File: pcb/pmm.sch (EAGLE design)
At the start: 38 parts, among them IC3 STM32F042F4, J1 AUDIO_JACK_3.5MM_PTH, J2 FFC3B07-05-T, SW3 324_SW, SW4 324_SW, U2 USBC_16P, U4 XC6206_DEV

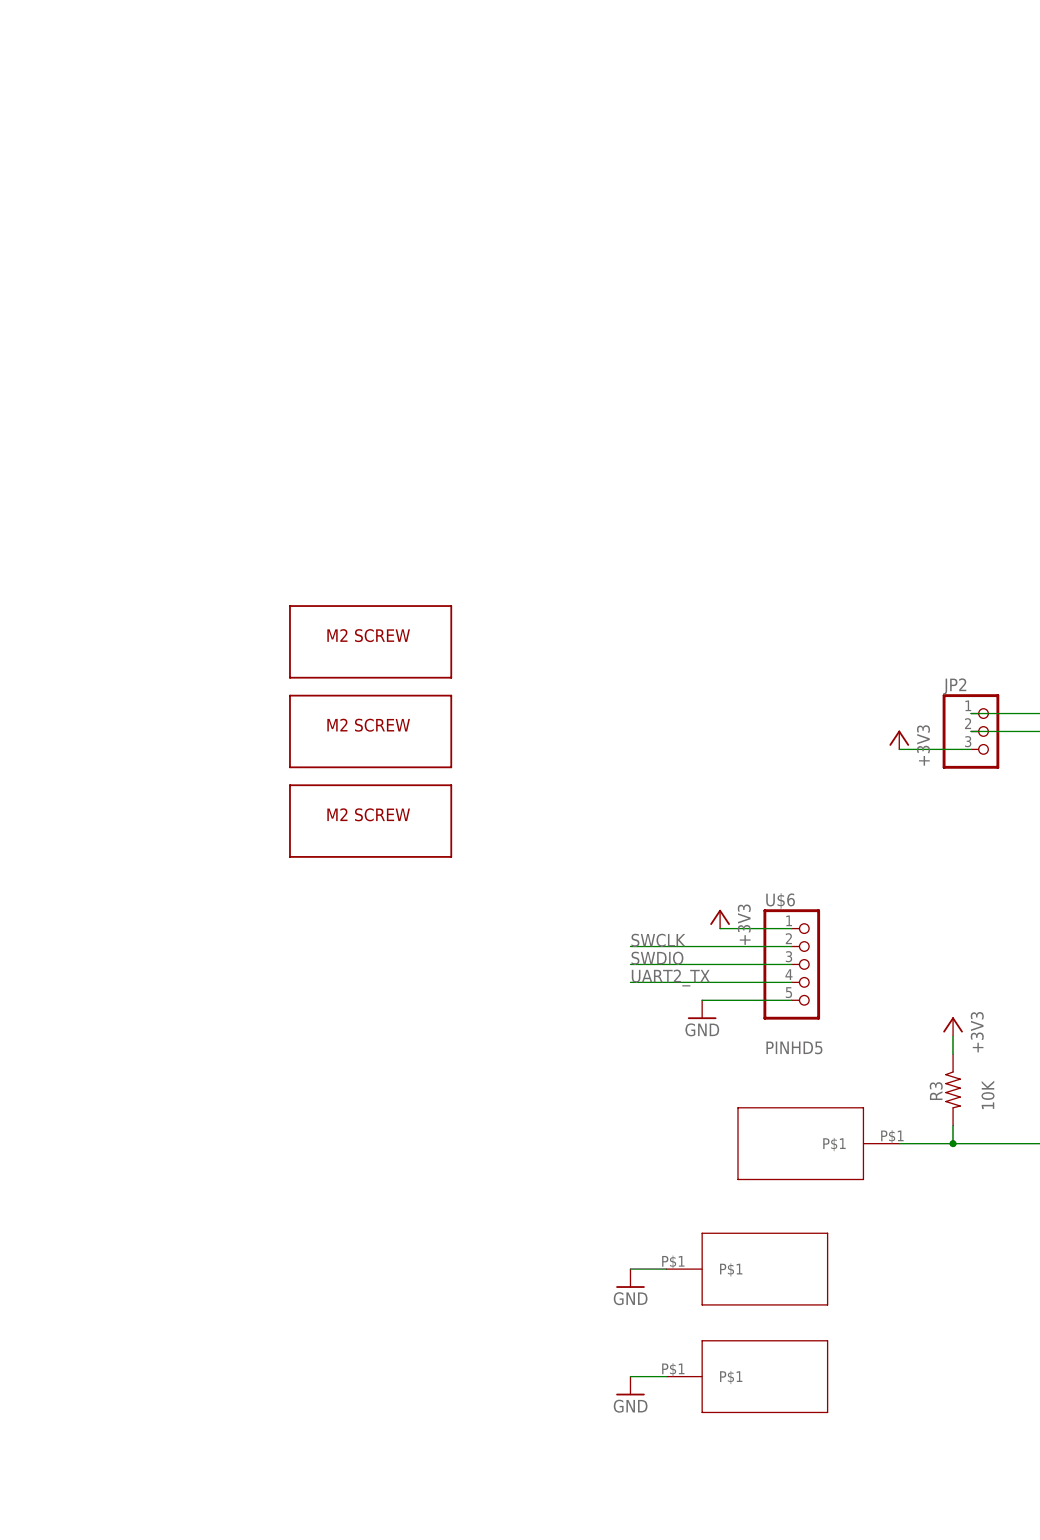
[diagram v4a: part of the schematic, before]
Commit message: added spring contacts
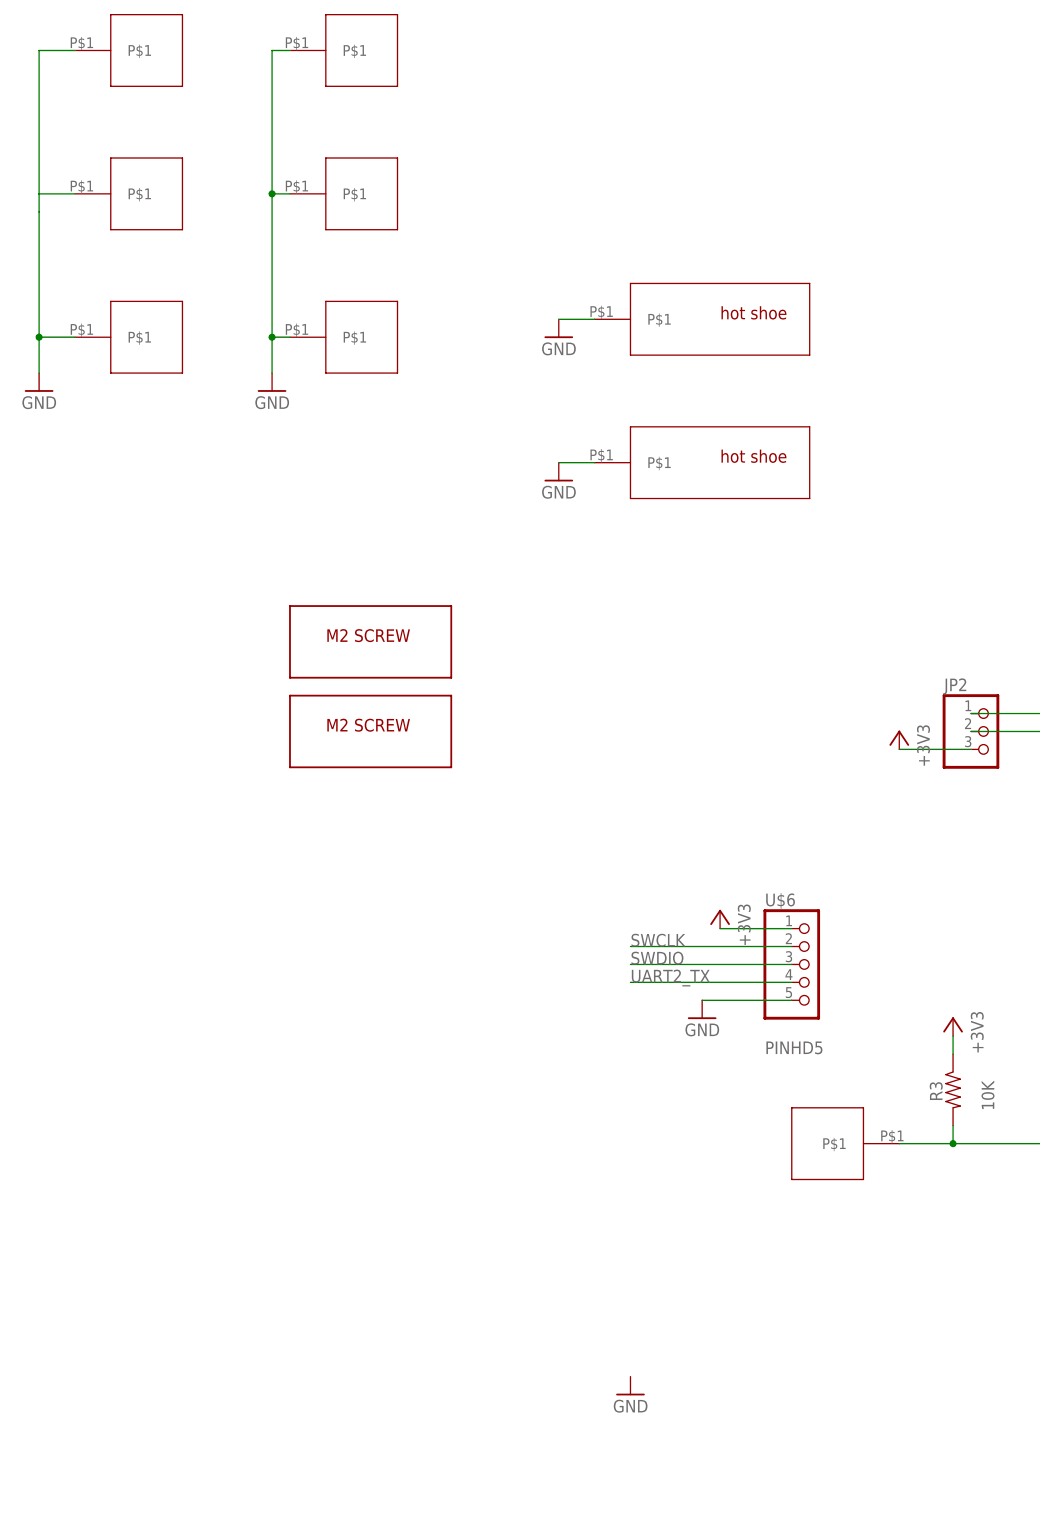
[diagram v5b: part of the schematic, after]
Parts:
- removed U$3: POGO_TH001, apricot:POGO_TH001
- added U$10, U$15: HOTSHOE, apricot:HOTSHOE
- added U$11, U$13, U$14, U$9: SPRING_CONTACT, apricot:SPRING_CONTACT
- U$2: value M2_SCREW_DEV -> SPRING_CONTACT; device 3pos_slide_switch_centered:M2_SCREW_DEV -> apricot:SPRING_CONTACT
- U$4, U$5: value POGO_TH001 -> SPRING_CONTACT; device apricot:POGO_TH001 -> apricot:SPRING_CONTACT
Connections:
- net GND: now also U$10.P$1, U$11.P$1, U$13.P$1, U$14.P$1, U$15.P$1, U$9.P$1
- net N$2: now also U$2.P$1; no longer U$3.P$1
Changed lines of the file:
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@@
 <part name="U$12" library="3pos_slide_switch_centered" deviceset="M2_SCREW_DEV" device=""/>
 <part name="U$1" library="3pos_slide_switch_centered" deviceset="M2_SCREW_DEV" device=""/>
-<part name="U$2" library="3pos_slide_switch_centered" deviceset="M2_SCREW_DEV" device=""/>
-<part name="U$3" library="apricot" deviceset="POGO_TH001" device=""/>
-<part name="U$4" library="apricot" deviceset="POGO_TH001" device=""/>
-<part name="U$5" library="apricot" deviceset="POGO_TH001" device=""/>
 <part name="U1" library="lul" deviceset="LUL_DISP_OLED_UG-2864HSWEG01" device=""/>
 <part name="GND26" library="supply1" library_urn="urn:adsk.eagle:library:371" deviceset="GND" device=""/>
@@
 <part name="R9" library="joyAnalog" deviceset="RESISTOR" device="0805-RES" value="10K"/>
 <part name="GND21" library="supply1" deviceset="GND" device=""/>
+<part name="U$11" library="apricot" deviceset="SPRING_CONTACT" device=""/>
+<part name="U$13" library="apricot" deviceset="SPRING_CONTACT" device=""/>
+<part name="U$14" library="apricot" deviceset="SPRING_CONTACT" device=""/>
+<part name="U$4" library="apricot" deviceset="SPRING_CONTACT" device=""/>
+<part name="U$5" library="apricot" deviceset="SPRING_CONTACT" device=""/>
+<part name="U$9" library="apricot" deviceset="SPRING_CONTACT" device=""/>
+<part name="GND22" library="supply1" deviceset="GND" device=""/>
+<part name="U$10" library="apricot" deviceset="HOTSHOE" device=""/>
+<part name="U$15" library="apricot" deviceset="HOTSHOE" device=""/>
+<part name="GND23" library="supply1" deviceset="GND" device=""/>
+<part name="GND24" library="supply1" deviceset="GND" device=""/>
+<part name="U$2" library="apricot" deviceset="SPRING_CONTACT" device=""/>
 </parts>
 <sheets>
@@
 <instance part="U$12" gate="G$1" x="-144.78" y="78.74" smashed="yes"/>
 <instance part="U$1" gate="G$1" x="-144.78" y="66.04" smashed="yes"/>
-<instance part="U$2" gate="G$1" x="-144.78" y="53.34" smashed="yes"/>
-<instance part="U$3" gate="G$1" x="-81.28" y="7.62" smashed="yes" rot="R180"/>
-<instance part="U$4" gate="G$1" x="-88.9" y="-10.16" smashed="yes"/>
-<instance part="U$5" gate="G$1" x="-88.9" y="-25.4" smashed="yes"/>
 <instance part="U1" gate="G$1" x="60.96" y="137.16" smashed="yes">
 <attribute name="NAME" x="40.64" y="162.56" size="1.27" layer="95" font="vector"/>
@@
 <attribute name="VALUE" x="-5.08" y="53.34" size="1.778" layer="96"/>
 </instance>
-<instance part="GND2" gate="1" x="-106.68" y="-12.7" smashed="yes" rot="MR0">
-<attribute name="VALUE" x="-104.14" y="-15.24" size="1.778" layer="96" rot="MR0"/>
+<instance part="GND2" gate="1" x="-190.5" y="114.3" smashed="yes" rot="MR0">
+<attribute name="VALUE" x="-187.96" y="111.76" size="1.778" layer="96" rot="MR0"/>
 </instance>
 <instance part="GND3" gate="1" x="-106.68" y="-27.94" smashed="yes" rot="MR0">
@@
 <attribute name="VALUE" x="-25.4" y="53.34" size="1.778" layer="96" rot="MR0"/>
 </instance>
+<instance part="U$11" gate="G$1" x="-175.26" y="142.24" smashed="yes"/>
+<instance part="U$13" gate="G$1" x="-175.26" y="121.92" smashed="yes"/>
+<instance part="U$14" gate="G$1" x="-175.26" y="162.56" smashed="yes"/>
+<instance part="U$4" gate="G$1" x="-144.78" y="142.24" smashed="yes"/>
+<instance part="U$5" gate="G$1" x="-144.78" y="121.92" smashed="yes"/>
+<instance part="U$9" gate="G$1" x="-144.78" y="162.56" smashed="yes"/>
+<instance part="GND22" gate="1" x="-157.48" y="114.3" smashed="yes" rot="MR0">
+<attribute name="VALUE" x="-154.94" y="111.76" size="1.778" layer="96" rot="MR0"/>
+</instance>
+<instance part="U$10" gate="G$1" x="-101.6" y="124.46" smashed="yes"/>
+<instance part="U$15" gate="G$1" x="-101.6" y="104.14" smashed="yes"/>
+<instance part="GND23" gate="1" x="-116.84" y="101.6" smashed="yes" rot="MR0">
+<attribute name="VALUE" x="-114.3" y="99.06" size="1.778" layer="96" rot="MR0"/>
+</instance>
+<instance part="GND24" gate="1" x="-116.84" y="121.92" smashed="yes" rot="MR0">
+<attribute name="VALUE" x="-114.3" y="119.38" size="1.778" layer="96" rot="MR0"/>
+</instance>
+<instance part="U$2" gate="G$1" x="-78.74" y="7.62" smashed="yes" rot="R180"/>
 </instances>
 <busses>
@@
 <pinref part="R8" gate="G$1" pin="2"/>
 <pinref part="GND30" gate="1" pin="GND"/>
-</segment>
-<segment>
-<pinref part="GND2" gate="1" pin="GND"/>
-<pinref part="U$4" gate="G$1" pin="P$1"/>
-<wire x1="-106.68" y1="-10.16" x2="-101.6" y2="-10.16" width="0.1524" layer="91"/>
-</segment>
-<segment>
-<pinref part="GND3" gate="1" pin="GND"/>
-<pinref part="U$5" gate="G$1" pin="P$1"/>
-<wire x1="-106.68" y1="-25.4" x2="-101.6" y2="-25.4" width="0.1524" layer="91"/>
 </segment>
 <segment>
@@
 <pinref part="GND21" gate="1" pin="GND"/>
 </segment>
+<segment>
+<pinref part="GND2" gate="1" pin="GND"/>
+<pinref part="U$13" gate="G$1" pin="P$1"/>
+<wire x1="-190.5" y1="116.84" x2="-190.5" y2="121.92" width="0.1524" layer="91"/>
+<wire x1="-190.5" y1="121.92" x2="-185.42" y2="121.92" width="0.1524" layer="91"/>
+<pinref part="U$11" gate="G$1" pin="P$1"/>
+<wire x1="-185.42" y1="142.24" x2="-190.5" y2="142.24" width="0.1524" layer="91"/>
+<wire x1="-190.5" y1="142.24" x2="-190.5" y2="139.7" width="0.1524" layer="91"/>
+<junction x="-190.5" y="121.92"/>
+<pinref part="U$14" gate="G$1" pin="P$1"/>
+<wire x1="-190.5" y1="139.7" x2="-190.5" y2="121.92" width="0.1524" layer="91"/>
+<wire x1="-185.42" y1="162.56" x2="-190.5" y2="162.56" width="0.1524" layer="91"/>
+<wire x1="-190.5" y1="162.56" x2="-190.5" y2="142.24" width="0.1524" layer="91"/>
+</segment>
+<segment>
+<pinref part="U$5" gate="G$1" pin="P$1"/>
+<pinref part="GND22" gate="1" pin="GND"/>
+<wire x1="-154.94" y1="121.92" x2="-157.48" y2="121.92" width="0.1524" layer="91"/>
+<wire x1="-157.48" y1="121.92" x2="-157.48" y2="116.84" width="0.1524" layer="91"/>
+<pinref part="U$9" gate="G$1" pin="P$1"/>
+<wire x1="-154.94" y1="162.56" x2="-157.48" y2="162.56" width="0.1524" layer="91"/>
+<wire x1="-157.48" y1="162.56" x2="-157.48" y2="142.24" width="0.1524" layer="91"/>
+<junction x="-157.48" y="121.92"/>
+<pinref part="U$4" gate="G$1" pin="P$1"/>
+<wire x1="-157.48" y1="142.24" x2="-157.48" y2="121.92" width="0.1524" layer="91"/>
+<wire x1="-154.94" y1="142.24" x2="-157.48" y2="142.24" width="0.1524" layer="91"/>
+<junction x="-157.48" y="142.24"/>
+</segment>
+<segment>
+<pinref part="GND24" gate="1" pin="GND"/>
+<pinref part="U$10" gate="G$1" pin="P$1"/>
+<wire x1="-116.84" y1="124.46" x2="-111.76" y2="124.46" width="0.1524" layer="91"/>
+</segment>
+<segment>
+<pinref part="U$15" gate="G$1" pin="P$1"/>
+<pinref part="GND23" gate="1" pin="GND"/>
+<wire x1="-111.76" y1="104.14" x2="-116.84" y2="104.14" width="0.1524" layer="91"/>
+</segment>
 </net>
 <net name="+3V3" class="0">
@@
 <segment>
 <pinref part="IC3" gate="G$1" pin="PB1"/>
-<pinref part="U$3" gate="G$1" pin="P$1"/>
 <wire x1="-17.78" y1="7.62" x2="-33.02" y2="7.62" width="0.1524" layer="91"/>
 <pinref part="U$7" gate="1" pin="3"/>
@@
 <wire x1="-60.96" y1="10.16" x2="-60.96" y2="7.62" width="0.1524" layer="91"/>
 <junction x="-60.96" y="7.62"/>
-</segment>
-</net>
+<pinref part="U$2" gate="G$1" pin="P$1"/>
+</segment>
+</net>

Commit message: adjusted resistor values
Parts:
- R7: value 390K -> 270K
- R9: value 10K -> 270K
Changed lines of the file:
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@@
 <part name="GND26" library="supply1" library_urn="urn:adsk.eagle:library:371" deviceset="GND" device=""/>
 <part name="+3V14" library="supply1" library_urn="urn:adsk.eagle:library:371" deviceset="+3V3" device=""/>
-<part name="R7" library="SparkFun-Passives" deviceset="RESISTOR" device="0805-RES" value="390K"/>
+<part name="R7" library="SparkFun-Passives" deviceset="RESISTOR" device="0805-RES" value="270K"/>
 <part name="C20" library="clock" deviceset="CAP" device="0805" value="1uF"/>
 <part name="C21" library="clock" deviceset="CAP" device="0805" value="1uF"/>
@@
 <part name="JP2" library="adafruit_changed" deviceset="PINHD-1X3" device="CB"/>
 <part name="+3V9" library="supply1" library_urn="urn:adsk.eagle:library:371" deviceset="+3V3" device=""/>
-<part name="R9" library="joyAnalog" deviceset="RESISTOR" device="0805-RES" value="10K"/>
+<part name="R9" library="joyAnalog" deviceset="RESISTOR" device="0805-RES" value="270K"/>
 <part name="GND21" library="supply1" deviceset="GND" device=""/>
 <part name="U$11" library="apricot" deviceset="SPRING_CONTACT" device=""/>

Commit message: updated PCB
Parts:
- removed U$11, U$13, U$14, U$5, U$9: SPRING_CONTACT, apricot:SPRING_CONTACT
- added U$3: HOTSHOE, apricot:HOTSHOE
- U$4: value SPRING_CONTACT -> HOTSHOE; device apricot:SPRING_CONTACT -> apricot:HOTSHOE
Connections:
- net GND: now also U$3.P$1; no longer U$11.P$1, U$13.P$1, U$14.P$1, U$5.P$1, U$9.P$1
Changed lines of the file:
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@@
 <part name="J1" library="SparkFun-Connectors" deviceset="AUDIO_JACK_3.5MM" device="_PTH"/>
 <part name="J2" library="FFC3B07-05-T" deviceset="FFC3B07-05-T" device=""/>
-<part name="GND2" library="supply1" deviceset="GND" device=""/>
 <part name="GND3" library="supply1" deviceset="GND" device=""/>
 <part name="GND4" library="supply1" deviceset="GND" device=""/>
@@
 <part name="R9" library="joyAnalog" deviceset="RESISTOR" device="0805-RES" value="270K"/>
 <part name="GND21" library="supply1" deviceset="GND" device=""/>
-<part name="U$11" library="apricot" deviceset="SPRING_CONTACT" device=""/>
-<part name="U$13" library="apricot" deviceset="SPRING_CONTACT" device=""/>
-<part name="U$14" library="apricot" deviceset="SPRING_CONTACT" device=""/>
-<part name="U$4" library="apricot" deviceset="SPRING_CONTACT" device=""/>
-<part name="U$5" library="apricot" deviceset="SPRING_CONTACT" device=""/>
-<part name="U$9" library="apricot" deviceset="SPRING_CONTACT" device=""/>
-<part name="GND22" library="supply1" deviceset="GND" device=""/>
 <part name="U$10" library="apricot" deviceset="HOTSHOE" device=""/>
 <part name="U$15" library="apricot" deviceset="HOTSHOE" device=""/>
@@
 <part name="GND24" library="supply1" deviceset="GND" device=""/>
 <part name="U$2" library="apricot" deviceset="SPRING_CONTACT" device=""/>
+<part name="U$3" library="apricot" deviceset="HOTSHOE" device=""/>
+<part name="U$4" library="apricot" deviceset="HOTSHOE" device=""/>
+<part name="GND2" library="supply1" deviceset="GND" device=""/>
+<part name="GND22" library="supply1" deviceset="GND" device=""/>
 </parts>
 <sheets>
@@
 <attribute name="VALUE" x="-5.08" y="53.34" size="1.778" layer="96"/>
 </instance>
-<instance part="GND2" gate="1" x="-190.5" y="114.3" smashed="yes" rot="MR0">
-<attribute name="VALUE" x="-187.96" y="111.76" size="1.778" layer="96" rot="MR0"/>
-</instance>
 <instance part="GND3" gate="1" x="-106.68" y="-27.94" smashed="yes" rot="MR0">
 <attribute name="VALUE" x="-104.14" y="-30.48" size="1.778" layer="96" rot="MR0"/>
@@
 <attribute name="VALUE" x="-25.4" y="53.34" size="1.778" layer="96" rot="MR0"/>
 </instance>
-<instance part="U$11" gate="G$1" x="-175.26" y="142.24" smashed="yes"/>
-<instance part="U$13" gate="G$1" x="-175.26" y="121.92" smashed="yes"/>
-<instance part="U$14" gate="G$1" x="-175.26" y="162.56" smashed="yes"/>
-<instance part="U$4" gate="G$1" x="-144.78" y="142.24" smashed="yes"/>
-<instance part="U$5" gate="G$1" x="-144.78" y="121.92" smashed="yes"/>
-<instance part="U$9" gate="G$1" x="-144.78" y="162.56" smashed="yes"/>
-<instance part="GND22" gate="1" x="-157.48" y="114.3" smashed="yes" rot="MR0">
-<attribute name="VALUE" x="-154.94" y="111.76" size="1.778" layer="96" rot="MR0"/>
-</instance>
 <instance part="U$10" gate="G$1" x="-101.6" y="124.46" smashed="yes"/>
 <instance part="U$15" gate="G$1" x="-101.6" y="104.14" smashed="yes"/>
@@
 </instance>
 <instance part="U$2" gate="G$1" x="-78.74" y="7.62" smashed="yes" rot="R180"/>
+<instance part="U$3" gate="G$1" x="-101.6" y="162.56" smashed="yes"/>
+<instance part="U$4" gate="G$1" x="-101.6" y="142.24" smashed="yes"/>
+<instance part="GND2" gate="1" x="-116.84" y="139.7" smashed="yes" rot="MR0">
+<attribute name="VALUE" x="-114.3" y="137.16" size="1.778" layer="96" rot="MR0"/>
+</instance>
+<instance part="GND22" gate="1" x="-116.84" y="160.02" smashed="yes" rot="MR0">
+<attribute name="VALUE" x="-114.3" y="157.48" size="1.778" layer="96" rot="MR0"/>
+</instance>
 </instances>
 <busses>
@@
 </segment>
 <segment>
-<pinref part="GND2" gate="1" pin="GND"/>
-<pinref part="U$13" gate="G$1" pin="P$1"/>
-<wire x1="-190.5" y1="116.84" x2="-190.5" y2="121.92" width="0.1524" layer="91"/>
-<wire x1="-190.5" y1="121.92" x2="-185.42" y2="121.92" width="0.1524" layer="91"/>
-<pinref part="U$11" gate="G$1" pin="P$1"/>
-<wire x1="-185.42" y1="142.24" x2="-190.5" y2="142.24" width="0.1524" layer="91"/>
-<wire x1="-190.5" y1="142.24" x2="-190.5" y2="139.7" width="0.1524" layer="91"/>
-<junction x="-190.5" y="121.92"/>
-<pinref part="U$14" gate="G$1" pin="P$1"/>
-<wire x1="-190.5" y1="139.7" x2="-190.5" y2="121.92" width="0.1524" layer="91"/>
-<wire x1="-185.42" y1="162.56" x2="-190.5" y2="162.56" width="0.1524" layer="91"/>
-<wire x1="-190.5" y1="162.56" x2="-190.5" y2="142.24" width="0.1524" layer="91"/>
-</segment>
-<segment>
-<pinref part="U$5" gate="G$1" pin="P$1"/>
-<pinref part="GND22" gate="1" pin="GND"/>
-<wire x1="-154.94" y1="121.92" x2="-157.48" y2="121.92" width="0.1524" layer="91"/>
-<wire x1="-157.48" y1="121.92" x2="-157.48" y2="116.84" width="0.1524" layer="91"/>
-<pinref part="U$9" gate="G$1" pin="P$1"/>
-<wire x1="-154.94" y1="162.56" x2="-157.48" y2="162.56" width="0.1524" layer="91"/>
-<wire x1="-157.48" y1="162.56" x2="-157.48" y2="142.24" width="0.1524" layer="91"/>
-<junction x="-157.48" y="121.92"/>
-<pinref part="U$4" gate="G$1" pin="P$1"/>
-<wire x1="-157.48" y1="142.24" x2="-157.48" y2="121.92" width="0.1524" layer="91"/>
-<wire x1="-154.94" y1="142.24" x2="-157.48" y2="142.24" width="0.1524" layer="91"/>
-<junction x="-157.48" y="142.24"/>
-</segment>
-<segment>
 <pinref part="GND24" gate="1" pin="GND"/>
 <pinref part="U$10" gate="G$1" pin="P$1"/>
@@
 <wire x1="-111.76" y1="104.14" x2="-116.84" y2="104.14" width="0.1524" layer="91"/>
 </segment>
+<segment>
+<pinref part="GND22" gate="1" pin="GND"/>
+<pinref part="U$3" gate="G$1" pin="P$1"/>
+<wire x1="-116.84" y1="162.56" x2="-111.76" y2="162.56" width="0.1524" layer="91"/>
+</segment>
+<segment>
+<pinref part="U$4" gate="G$1" pin="P$1"/>
+<pinref part="GND2" gate="1" pin="GND"/>
+<wire x1="-111.76" y1="142.24" x2="-116.84" y2="142.24" width="0.1524" layer="91"/>
+</segment>
 </net>

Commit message: adjusted PCB
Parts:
- C2: value 100nF -> 2.2uF
- R4: value 5K1 -> 2K
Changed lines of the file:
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@@
 <part name="SW4" library="3pos_slide_switch_centered" deviceset="324_SW" device="" value="324_SW"/>
 <part name="LED1" library="adafruit" deviceset="LED" device="CHIP-LED0805"/>
-<part name="R4" library="SparkFun-Passives" deviceset="RESISTOR" device="0805-RES" value="5K1"/>
+<part name="R4" library="SparkFun-Passives" deviceset="RESISTOR" device="0805-RES" value="2K"/>
 <part name="+3V2" library="supply1" library_urn="urn:adsk.eagle:library:371" deviceset="+3V3" device=""/>
 <part name="R5" library="joyAnalog" deviceset="RESISTOR" device="0805-RES" value="10K"/>
 <part name="GND10" library="supply1" deviceset="GND" device=""/>
 <part name="U4" library="3pos_slide_switch" deviceset="XC6206_DEV" device=""/>
-<part name="C2" library="clock" deviceset="CAP" device="0805" value="100nF"/>
+<part name="C2" library="clock" deviceset="CAP" device="0805" value="2.2uF"/>
 <part name="+3V3" library="supply1" library_urn="urn:adsk.eagle:library:371" deviceset="+3V3" device=""/>
 <part name="U$12" library="3pos_slide_switch_centered" deviceset="M2_SCREW_DEV" device=""/>
